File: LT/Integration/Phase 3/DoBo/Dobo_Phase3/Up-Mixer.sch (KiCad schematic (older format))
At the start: 16 parts, among them J8 Conn_Coaxial, T3 3:16, T4 8:1, U2 SA602

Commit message: Added the completed layout for the DoBo Phase 3
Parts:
- removed R39: 0, Resistor_SMD:R_0805_2012Metric_Pad1.15x1.40mm_HandSolder, symbol Device:R
- removed T3: 3:16, symbol Device:Transformer_1P_1S
- removed T4: 8:1, symbol Device:Transformer_1P_1S
- added T3, T4: Transformer_6, LT:PWB1040L, symbol LT-Schematics:Transformer_6
- J8: footprint Connector_Coaxial:SMA_Amphenol_132289_EdgeMount -> Connector_Coaxial:SMA_Amphenol_132291_Vertical
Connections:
- net labels added: +8V, Local_Oscillator_Output, Up_Mixer_input
- net labels removed: 40.1_LO_output, VCC, VGA_output
- no-connect marks 1 -> 5
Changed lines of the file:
@@
 $Descr A4 11693 8268
 encoding utf-8
-Sheet 4 10
+Sheet 9 10
 Title ""
 Date ""
@@
 $EndComp
 $Comp
-L Device:Transformer_1P_1S T3
-U 1 1 5E44A49C
-P 3700 3950
-F 0 "T3" H 3700 4331 50  0000 C CNN
-F 1 "3:16" H 3700 4240 50  0000 C CNN
-F 2 "" H 3700 3950 50  0001 C CNN
-F 3 "~" H 3700 3950 50  0001 C CNN
-	1    3700 3950
-	1    0    0    -1
-$EndComp
-$Comp
 L LT-Schematics:SA602 U2
 U 1 1 5E447907
@@
 	0    -1   1    0
 $EndComp
-$Comp
-L Device:Transformer_1P_1S T4
-U 1 1 5EAF5C80
-P 7350 4050
-F 0 "T4" H 7350 4431 50  0000 C CNN
-F 1 "8:1" H 7350 4340 50  0000 C CNN
-F 2 "" H 7350 4050 50  0001 C CNN
-F 3 "~" H 7350 4050 50  0001 C CNN
-	1    7350 4050
-	-1   0    0    -1
-$EndComp
 Wire Wire Line
 	6450 3950 6450 3850
@@
 F 0 "J8" H 8328 4088 50  0000 C CNN
 F 1 "Conn_Coaxial" H 8328 3997 50  0000 C CNN
-F 2 "Connector_Coaxial:SMA_Amphenol_132289_EdgeMount" H 8400 3850 50  0001 C CNN
+F 2 "Connector_Coaxial:SMA_Amphenol_132291_Vertical" H 8400 3850 50  0001 C CNN
 F 3 " ~" H 8400 3850 50  0001 C CNN
 	1    8400 3850
@@
 Wire Wire Line
 	6150 2650 6300 2650
-$Comp
-L power:VCC #PWR015
-U 1 1 5E466840
-P 5450 3300
-F 0 "#PWR015" H 5450 3150 50  0001 C CNN
-F 1 "VCC" H 5467 3473 50  0000 C CNN
-F 2 "" H 5450 3300 50  0001 C CNN
-F 3 "" H 5450 3300 50  0001 C CNN
-	1    5450 3300
-	1    0    0    -1
-$EndComp
 Wire Wire Line
 	5450 3300 5450 3350
@@
 $EndComp
 Text HLabel 2500 3750 0    50   Input ~ 0
-VGA_output
+Up_Mixer_input
 Wire Wire Line
 	2550 3750 2500 3750
 Text HLabel 5250 2650 0    50   Input ~ 0
-40.1_LO_output
+Local_Oscillator_Output
 Wire Wire Line
 	5250 2650 5300 2650
-$Comp
-L Device:R R39
-U 1 1 5EB1E0C7
-P 7900 3850
-F 0 "R39" V 7693 3850 50  0000 C CNN
-F 1 "0" V 7784 3850 50  0000 C CNN
-F 2 "Resistor_SMD:R_0805_2012Metric_Pad1.15x1.40mm_HandSolder" V 7830 3850 50  0001 C CNN
-F 3 "~" H 7900 3850 50  0001 C CNN
-	1    7900 3850
-	0    1    1    0
-$EndComp
 $Comp
 L Device:R R14
@@
 	8100 4700 8250 4700
 Connection ~ 8100 3850
-Wire Wire Line
-	8100 3850 8050 3850
+$Comp
+L LT-Schematics:Transformer_6 T3
+U 1 1 5EEB8053
+P 3700 3950
+F 0 "T3" H 3700 4331 50  0000 C CNN
+F 1 "Transformer_6" H 3700 4240 50  0000 C CNN
+F 2 "LT:PWB1040L" H 3700 3950 50  0001 C CNN
+F 3 "~" H 3700 3950 50  0001 C CNN
+	1    3700 3950
+	1    0    0    -1
+$EndComp
+$Comp
+L LT-Schematics:Transformer_6 T4
+U 1 1 5EEB9294
+P 7350 4050
+F 0 "T4" H 7350 4431 50  0000 C CNN
+F 1 "Transformer_6" H 7350 4340 50  0000 C CNN
+F 2 "LT:PWB1040L" H 7350 4050 50  0001 C CNN
+F 3 "~" H 7350 4050 50  0001 C CNN
+	1    7350 4050
+	-1   0    0    -1
+$EndComp
+NoConn ~ 6950 4050
+NoConn ~ 7750 4050
+NoConn ~ 3300 3950
+NoConn ~ 4100 3950
+Wire Wire Line
+	7750 3850 8100 3850
+$Comp
+L power:+8V #PWR0135
+U 1 1 5EF04367
+P 5450 3300
+F 0 "#PWR0135" H 5450 3150 50  0001 C CNN
+F 1 "+8V" H 5465 3473 50  0000 C CNN
+F 2 "" H 5450 3300 50  0001 C CNN
+F 3 "" H 5450 3300 50  0001 C CNN
+	1    5450 3300
+	1    0    0    -1
+$EndComp
 $EndSCHEMATC

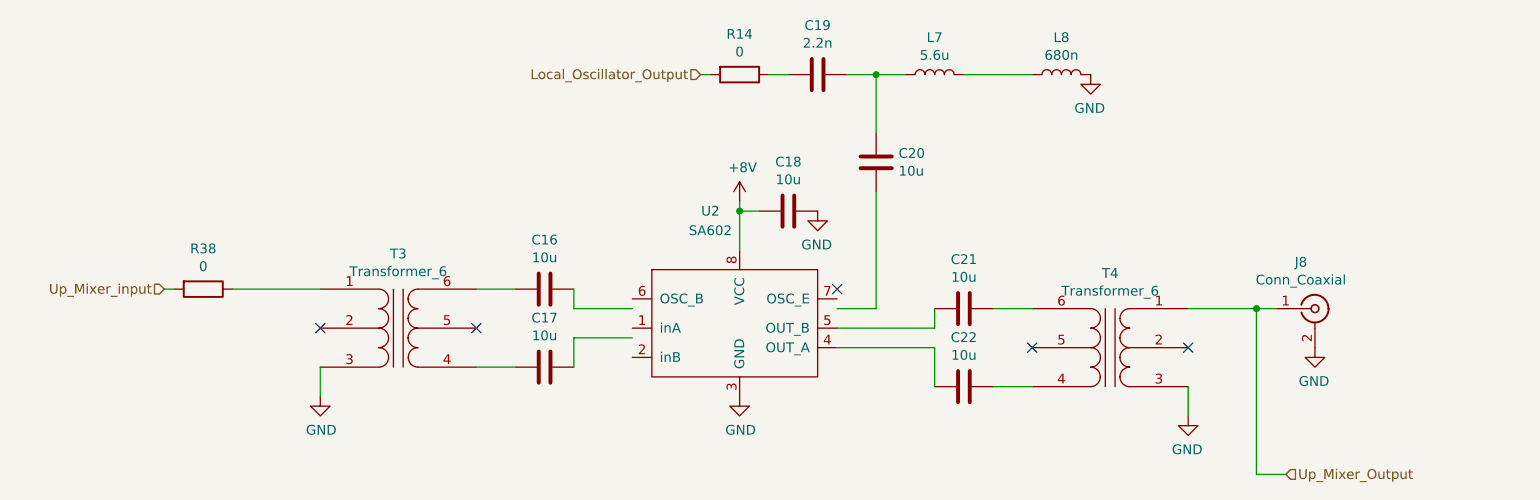
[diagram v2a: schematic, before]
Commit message: Adding the DoBo Phase 3 integration with all traces routed
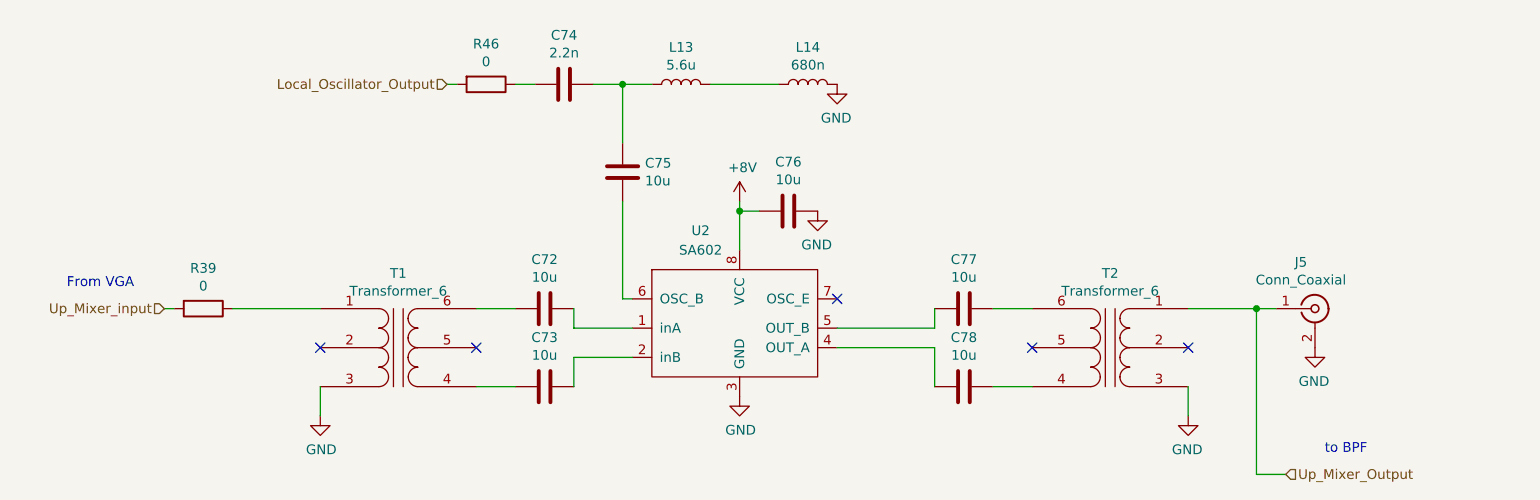
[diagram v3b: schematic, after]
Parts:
- renumbered C16 to C72, C17 to C73, C19 to C74, C20 to C75, C18 to C76, C21 to C77, C22 to C78, J8 to J5, L7 to L13, L8 to L14, R38 to R39, R14 to R46, T3 to T1, T4 to T2
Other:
- note added: "From VGA"
- note added: "to BPF"
- moved on the sheet: C72, C73, C74, C75, L13, L14, R39, R46, T1

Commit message: Fixed the hierarchy for the MoBo Phase 3
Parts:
- U2: symbol LT-Schematics:SA602 -> Dobo_Phase3-rescue:SA602-LT-Schematics
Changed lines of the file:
@@
 $EndComp
 $Comp
-L LT-Schematics:SA602 U2
+L Dobo_Phase3-rescue:SA602-LT-Schematics U2
 U 1 1 5EBBC760
 P 5000 3750

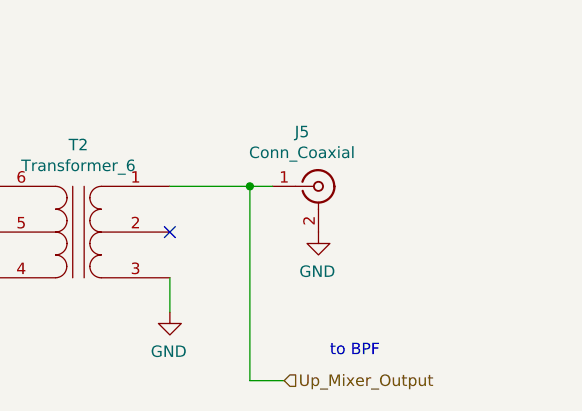
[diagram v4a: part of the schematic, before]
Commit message: Added the finalized layouts for the Mobo and Dobo Phase 3, as well as the preliminary layout for Phase 4 of both boards
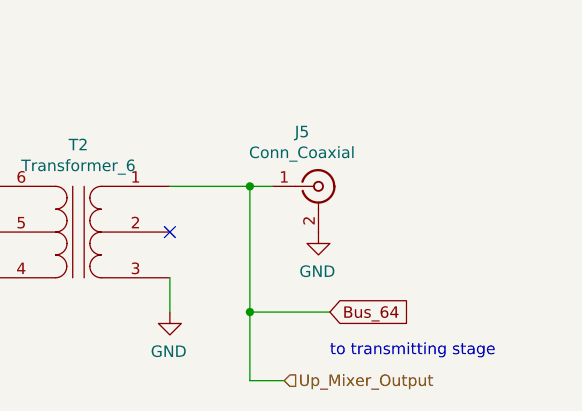
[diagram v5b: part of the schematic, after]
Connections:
- net Up_Mixer_Output renamed Bus_64
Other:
- note added: "to transmitting stage"
- note removed: "to BPF"
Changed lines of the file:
@@
 $Descr A4 11693 8268
 encoding utf-8
-Sheet 7 10
+Sheet 10 10
 Title ""
 Date ""
@@
 Up_Mixer_Output
 Wire Wire Line
-	8100 3850 8100 4700
+	8100 3850 8100 4400
 Wire Wire Line
 	8100 4700 8250 4700
@@
 From VGA
 Text Notes 8450 4600 0    50   ~ 0
-to BPF
+to transmitting stage
+Text GLabel 8450 4400 2    50   Input ~ 0
+Bus_64
+Wire Wire Line
+	8450 4400 8100 4400
+Connection ~ 8100 4400
+Wire Wire Line
+	8100 4400 8100 4700
 $EndSCHEMATC
